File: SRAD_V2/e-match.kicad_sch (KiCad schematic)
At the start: 28 parts, among them IC1 NCV81071BZR2G, IC2 NCV81071BZR2G, J2 691210910002, J3 691210910002, J4 691210910002, J5 691210910002, Q1 FDS6630A, Q2 FDS6630A, Q3 RQ6E080AJ, Q4 RQ6E080AJ, U3 TMCS1108A2UQDR

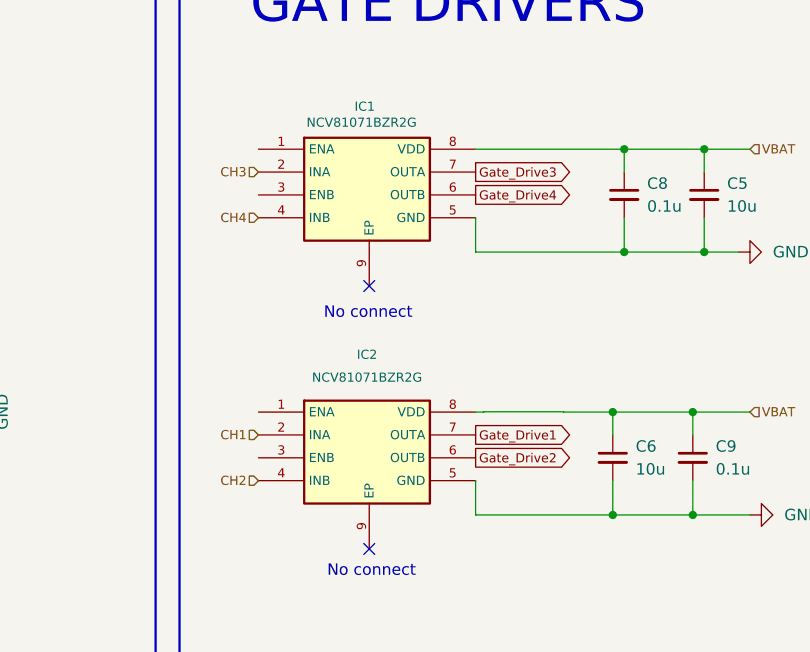
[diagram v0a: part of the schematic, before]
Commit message: routing for e-match circuit
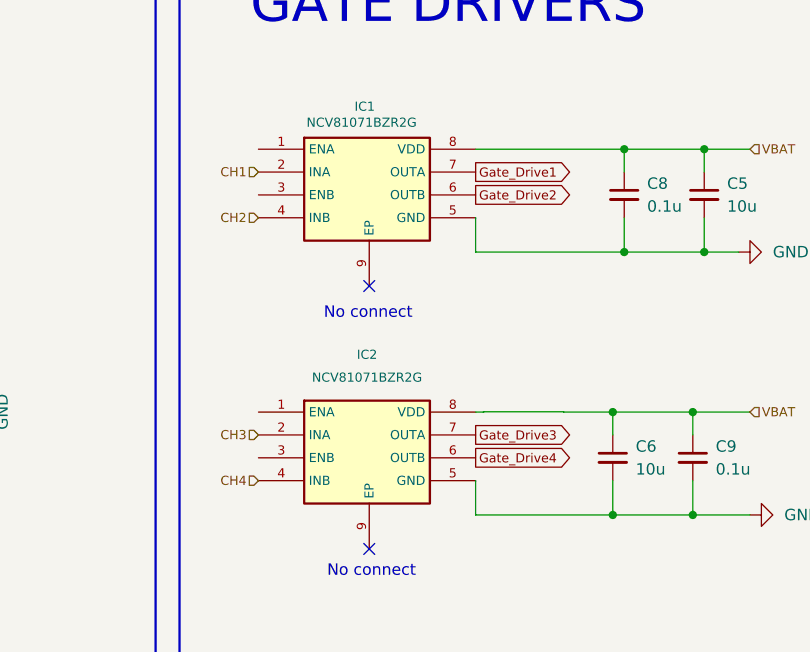
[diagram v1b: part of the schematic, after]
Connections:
- net CH1: now also IC1.2 (INA); no longer IC2.2 (INA)
- net CH2: now also IC1.4 (INB); no longer IC2.4 (INB)
- net CH3: now also IC2.2 (INA); no longer IC1.2 (INA)
- net CH4: now also IC2.4 (INB); no longer IC1.4 (INB)
- net Gate_Drive1: now also IC1.7 (OUTA); no longer IC2.7 (OUTA)
- net Gate_Drive2: now also IC1.6 (OUTB); no longer IC2.6 (OUTB)
- net Gate_Drive3: now also IC2.7 (OUTA); no longer IC1.7 (OUTA)
- net Gate_Drive4: now also IC2.6 (OUTB); no longer IC1.6 (OUTB)

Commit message: sensor routing
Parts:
- C7, C8, C9: value 0.1u -> 100n
- CR1, CR2, CR3, CR4: footprint DIODE_MSP3V3 -> Schottky_Diode:DIODE_MSP3V3
- IC1, IC2: footprint SOP65P490X110-9N -> Gate_Driver:SOP65P490X110-9N
- LED1: footprint LED_LTST-C170GKT_LTO -> Smd_Led:LED_LTST-C170GKT_LTO
- Q1, Q2: value FDS6630A -> AOSP36326C
- Q3, Q4: value RQ6E080AJ -> FDC8878
- U3: footprint D0008A-IPC_A -> Current_Sensor:D0008A-IPC_A
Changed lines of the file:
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@@
 			)
 		)
-		(property "Value" "0.1u"
+		(property "Value" "100n"
 			(at 184.15 78.7462 0)
 			(show_name no)
@@
 			)
 		)
-		(property "Footprint" "DIODE_MSP3V3"
+		(property "Footprint" "Schottky_Diode:DIODE_MSP3V3"
 			(at 63.5 92.71 0)
 			(hide yes)
@@
 			)
 		)
-		(property "Value" "0.1u"
+		(property "Value" "100n"
 			(at 176.53 49.5362 0)
 			(show_name no)
@@
 			)
 		)
-		(property "Footprint" "D0008A-IPC_A"
+		(property "Footprint" "Current_Sensor:D0008A-IPC_A"
 			(at 46.99 57.15 0)
 			(hide yes)
@@
 			)
 		)
-		(property "Value" "FDS6630A"
-			(at 32.258 102.87 0)
+		(property "Value" "AOSP36326C"
+			(at 28.956 102.616 0)
 			(show_name no)
 			(do_not_autoplace no)
@@
 			)
 		)
-		(property "Value" "FDS6630A"
-			(at 51.308 102.87 0)
+		(property "Value" "AOSP36326C"
+			(at 49.022 102.87 0)
 			(show_name no)
 			(do_not_autoplace no)
@@
 			)
 		)
-		(property "Footprint" "LED_LTST-C170GKT_LTO"
+		(property "Footprint" "Smd_Led:LED_LTST-C170GKT_LTO"
 			(at 219.71 66.04 0)
 			(hide yes)
@@
 			)
 		)
-		(property "Footprint" "DIODE_MSP3V3"
+		(property "Footprint" "Schottky_Diode:DIODE_MSP3V3"
 			(at 82.55 92.71 0)
 			(hide yes)
@@
 			)
 		)
-		(property "Footprint" "DIODE_MSP3V3"
+		(property "Footprint" "Schottky_Diode:DIODE_MSP3V3"
 			(at 100.33 92.71 0)
 			(hide yes)
@@
 			)
 		)
-		(property "Footprint" "SOP65P490X110-9N"
+		(property "Footprint" "Gate_Driver:SOP65P490X110-9N"
 			(at 160.02 167.31 0)
 			(hide yes)
@@
 			)
 		)
-		(property "Value" "RQ6E080AJ"
+		(property "Value" "FDC8878"
 			(at 69.596 103.124 0)
 			(show_name no)
@@
 			)
 		)
-		(property "Footprint" "SOP65P490X110-9N"
+		(property "Footprint" "Gate_Driver:SOP65P490X110-9N"
 			(at 160.02 138.1 0)
 			(hide yes)
@@
 			)
 		)
-		(property "Value" "0.1u"
+		(property "Value" "100n"
 			(at 96.52 63.5062 0)
 			(show_name no)
@@
 			)
 		)
-		(property "Value" "RQ6E080AJ"
+		(property "Value" "FDC8878"
 			(at 88.392 102.87 0)
 			(show_name no)
@@
 			)
 		)
-		(property "Footprint" "DIODE_MSP3V3"
+		(property "Footprint" "Schottky_Diode:DIODE_MSP3V3"
 			(at 45.72 92.71 0)
 			(hide yes)

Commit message: Sensor routing and integration of various systems on the PCB
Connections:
- net IN(-): now reaches CR1.1, CR2.1, CR3.1, CR4.1, J2.2, J3.2, J4.2, J5.2, U3.3 (IN-), U3.4 (IN-)
- net Drain: now reaches CR2.2, J3.1, Q2.5 (D), Q2.6 (D), Q2.7 (D), Q2.8 (D)
- net Drain: now also CR1.2, CR3.2, CR4.2, J2.1, J4.1, J5.1, Q1.5 (D), Q1.6 (D), Q1.7 (D), Q1.8 (D), Q3.1 (D), Q3.2 (D), Q3.5 (D), Q3.6 (D), Q4.1 (D), Q4.2 (D), Q4.5 (D), Q4.6 (D)
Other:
- note removed: "Drain"
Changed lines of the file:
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@@
-		)
-	)
-	(text "Drain"
-		(exclude_from_sim no)
-		(at 61.8422 97.5285 90)
-		(effects
-			(font
-				(size 1.27 1.27)
-			)
-		)
-	)
-	(text "Drain"
-		(exclude_from_sim no)
-		(at 42.418 97.79 90)
-		(effects
-			(font
-				(size 1.27 1.27)
-			)
 		)
 	)
@@
 		)
 	)
-	(text "Drain"
-		(exclude_from_sim no)
-		(at 80.7974 97.5285 90)
-		(effects
-			(font
-				(size 1.27 1.27)
-			)
-		)
-	)
 	(text "Source"
 		(exclude_from_sim no)
@@
 		)
 	)
-	(text "Drain"
-		(exclude_from_sim no)
-		(at 100.33 97.79 90)
-		(effects
-			(font
-				(size 1.27 1.27)
-			)
-		)
-	)
 	(junction
 		(at 86.36 55.88)
@@
 	)
 	(junction
+		(at 76.2 82.55)
+		(diameter 0)
+		(color 0 0 0 0)
+	)
+	(junction
+		(at 57.15 82.55)
+		(diameter 0)
+		(color 0 0 0 0)
+	)
+	(junction
+		(at 93.98 71.12)
+		(diameter 0)
+		(color 0 0 0 0)
+	)
+	(junction
 		(at 34.29 57.15)
-		(diameter 0)
-		(color 0 0 0 0)
-	)
-	(junction
-		(at 76.2 82.55)
-		(diameter 0)
-		(color 0 0 0 0)
-	)
-	(junction
-		(at 57.15 82.55)
-		(diameter 0)
-		(color 0 0 0 0)
-	)
-	(junction
-		(at 93.98 71.12)
 		(diameter 0)
 		(color 0 0 0 0)
@@
 	(wire
 		(pts
+			(xy 30.48 57.15) (xy 34.29 57.15)
+		)
+		(stroke
+			(width 0)
+			(type default)
+		)
+	)
+	(wire
+		(pts
 			(xy 76.2 82.55) (xy 82.55 82.55)
 		)
@@
 	(wire
 		(pts
-			(xy 34.29 55.88) (xy 34.29 57.15)
-		)
-		(stroke
-			(width 0)
-			(type default)
-		)
-	)
-	(wire
-		(pts
 			(xy 187.96 83.82) (xy 181.61 83.82)
 		)
@@
 	(wire
 		(pts
-			(xy 31.75 54.61) (xy 31.75 55.88)
-		)
-		(stroke
-			(width 0)
-			(type default)
-		)
-	)
-	(wire
-		(pts
 			(xy 157.48 43.18) (xy 173.99 43.18)
 		)
@@
 	(wire
 		(pts
-			(xy 31.75 55.88) (xy 34.29 55.88)
-		)
-		(stroke
-			(width 0)
-			(type default)
-		)
-	)
-	(wire
-		(pts
 			(xy 182.88 54.61) (xy 186.69 54.61)
 		)
@@
 			(width 0)
 			(type default)
+		)
+	)
+	(label "IN(-)"
+		(at 46.99 76.2 0)
+		(effects
+			(font
+				(size 1.27 1.27)
+			)
+			(justify left bottom)
+		)
+	)
+	(label "IN(+)"
+		(at 31.75 57.15 0)
+		(effects
+			(font
+				(size 1.27 1.27)
+			)
+			(justify left bottom)
+		)
+	)
+	(label "Drain"
+		(at 44.45 97.79 0)
+		(effects
+			(font
+				(size 1.27 1.27)
+			)
+			(justify left bottom)
+		)
+	)
+	(label "Drain"
+		(at 101.6 97.79 0)
+		(effects
+			(font
+				(size 1.27 1.27)
+			)
+			(justify left bottom)
+		)
+	)
+	(label "Drain"
+		(at 82.55 97.79 0)
+		(effects
+			(font
+				(size 1.27 1.27)
+			)
+			(justify left bottom)
+		)
+	)
+	(label "Drain"
+		(at 63.5 97.79 0)
+		(effects
+			(font
+				(size 1.27 1.27)
+			)
+			(justify left bottom)
 		)
 	)
@@
 	(hierarchical_label "VBAT"
 		(shape input)
-		(at 31.75 54.61 90)
+		(at 30.48 57.15 180)
 		(effects
 			(font
 				(size 1.27 1.27)
 			)
-			(justify left)
-		)
-	)
+			(justify right)
+		)
+	)

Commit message: more routing
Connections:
- net 5V renamed +3.3V
- net VBAT renamed +BATT
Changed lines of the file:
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@@
-		)
-	)
-	(global_label "5V"
-		(shape input)
-		(at 100.33 55.88 0)
-		(fields_autoplaced yes)
-		(effects
-			(font
-				(size 1.016 1.016)
-			)
-			(justify left)
-		)
-		(property "Intersheetrefs" "${INTERSHEET_REFS}"
-			(at 104.5564 55.88 0)
-			(hide yes)
-			(show_name no)
-			(do_not_autoplace no)
-			(effects
-				(font
-					(size 1.27 1.27)
-				)
-				(justify left)
-			)
-		)
-	)
-	(global_label "5V"
-		(shape input)
-		(at 219.71 44.45 90)
-		(fields_autoplaced yes)
-		(effects
-			(font
-				(size 1.27 1.27)
-			)
-			(justify left)
-		)
-		(property "Intersheetrefs" "${INTERSHEET_REFS}"
-			(at 219.71 39.1667 90)
-			(hide yes)
-			(show_name no)
-			(do_not_autoplace no)
-			(effects
-				(font
-					(size 1.27 1.27)
-				)
-				(justify left)
-			)
 		)
 	)
@@
 		)
 	)
-	(hierarchical_label "VBAT"
+	(hierarchical_label "+BATT"
 		(shape input)
 		(at 187.96 72.39 0)
@@
 		)
 	)
-	(hierarchical_label "VBAT"
-		(shape input)
-		(at 30.48 57.15 180)
-		(effects
-			(font
-				(size 1.27 1.27)
-			)
-			(justify right)
-		)
-	)
-	(hierarchical_label "VBAT"
+	(hierarchical_label "+BATT"
 		(shape input)
 		(at 187.96 43.18 0)
@@
 			)
 			(justify left)
+		)
+	)
+	(hierarchical_label "+BATT"
+		(shape input)
+		(at 30.48 57.15 180)
+		(effects
+			(font
+				(size 1.016 1.016)
+			)
+			(justify right)
 		)
 	)
@@
 	)
 	(symbol
+		(lib_id "power:+3.3V")
+		(at 219.71 44.45 0)
+		(unit 1)
+		(body_style 1)
+		(exclude_from_sim no)
+		(in_bom yes)
+		(on_board yes)
+		(in_pos_files yes)
+		(dnp no)
+		(fields_autoplaced yes)
+		(property "Reference" "#PWR040"
+			(at 219.71 48.26 0)
+			(hide yes)
+			(show_name no)
+			(do_not_autoplace no)
+			(effects
+				(font
+					(size 1.27 1.27)
+				)
+			)
+		)
+		(property "Value" "+3.3V"
+			(at 219.71 39.37 0)
+			(show_name no)
+			(do_not_autoplace no)
+			(effects
+				(font
+					(size 1.27 1.27)
+				)
+			)
+		)
+		(property "Footprint" ""
+			(at 219.71 44.45 0)
+			(hide yes)
+			(show_name no)
+			(do_not_autoplace no)
+			(effects
+				(font
+					(size 1.27 1.27)
+				)
+			)
+		)
+		(property "Datasheet" ""
+			(at 219.71 44.45 0)
+			(hide yes)
+			(show_name no)
+			(do_not_autoplace no)
+			(effects
+				(font
+					(size 1.27 1.27)
+				)
+			)
+		)
+		(property "Description" "Power symbol creates a global label with name \"+3.3V\""
+			(at 219.71 44.45 0)
+			(hide yes)
+			(show_name no)
+			(do_not_autoplace no)
+			(effects
+				(font
+					(size 1.27 1.27)
+				)
+			)
+		)
+		(pin "1"
+		)
+		(instances
+			(project "SRAD_V2"
+				(path "/016ea6e5-09c6-43d4-b6cc-3404e2d65458/a2059f4c-c92f-483b-9b86-061767cb943d"
+					(reference "#PWR040")
+					(unit 1)
+				)
+			)
+		)
+	)
+	(symbol
 		(lib_id "power:GND")
 		(at 100.33 71.12 90)
@@
 					(unit 1)
 				)
+			)
+		)
+	)
+	(symbol
+		(lib_id "power:+3.3V")
+		(at 100.33 55.88 270)
+		(unit 1)
+		(body_style 1)
+		(exclude_from_sim no)
+		(in_bom yes)
+		(on_board yes)
+		(in_pos_files yes)
+		(dnp no)
+		(fields_autoplaced yes)
+		(property "Reference" "#PWR039"
+			(at 96.52 55.88 0)
+			(hide yes)
+			(show_name no)
+			(do_not_autoplace no)
+			(effects
+				(font
+					(size 1.27 1.27)
+				)
+			)
+		)
+		(property "Value" "+3.3V"
+			(at 104.14 55.8799 90)
+			(show_name no)
+			(do_not_autoplace no)
+			(effects
+				(font
+					(size 1.27 1.27)
+				)
+				(justify left)
+			)
+		)
+		(property "Footprint" ""
+			(at 100.33 55.88 0)
+			(hide yes)
+			(show_name no)
+			(do_not_autoplace no)
+			(effects
+				(font
+					(size 1.27 1.27)
+				)
+			)
+		)
+		(property "Datasheet" ""
+			(at 100.33 55.88 0)
+			(hide yes)
+			(show_name no)
+			(do_not_autoplace no)
+			(effects
+				(font
+					(size 1.27 1.27)
+				)
+			)
+		)
+		(property "Description" "Power symbol creates a global label with name \"+3.3V\""
+			(at 100.33 55.88 0)
+			(hide yes)
+			(show_name no)
+			(do_not_autoplace no)
+			(effects
+				(font
+					(size 1.27 1.27)
+				)
+			)
+		)
+		(pin "1"
+		)
+		(instances
+			(project "SRAD_V2"
+				(path "/016ea6e5-09c6-43d4-b6cc-3404e2d65458/a2059f4c-c92f-483b-9b86-061767cb943d"
+					(reference "#PWR039")
+					(unit 1)
+				)

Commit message: Updated the buzzer
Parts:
- C5, C6: footprint Capacitor_SMD:C_0603_1608Metric -> Capacitor_SMD:C_1210_3225Metric
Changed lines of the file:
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@@
 			)
 		)
-		(property "Footprint" "Capacitor_SMD:C_0603_1608Metric"
+		(property "Footprint" "Capacitor_SMD:C_1210_3225Metric"
 			(at 182.88 48.26 0)
 			(hide yes)
@@
 			)
 		)
-		(property "Footprint" "Capacitor_SMD:C_0603_1608Metric"
+		(property "Footprint" "Capacitor_SMD:C_1210_3225Metric"
 			(at 172.72 77.47 0)
 			(hide yes)
